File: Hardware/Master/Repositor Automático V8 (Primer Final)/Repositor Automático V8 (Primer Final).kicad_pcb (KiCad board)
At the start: 2 copper layers, 80.2 x 59.8 mm, 57 parts, among them IC1 TB67H450AFNG,EL, IC2 TB67H450AFNG,EL, IC3 TB67H450AFNG,EL, IC4 MP2307, J11 FdC, J2 UART, J3 Motor2, J4 Motor1, J5 Motor3, J6 Motor4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

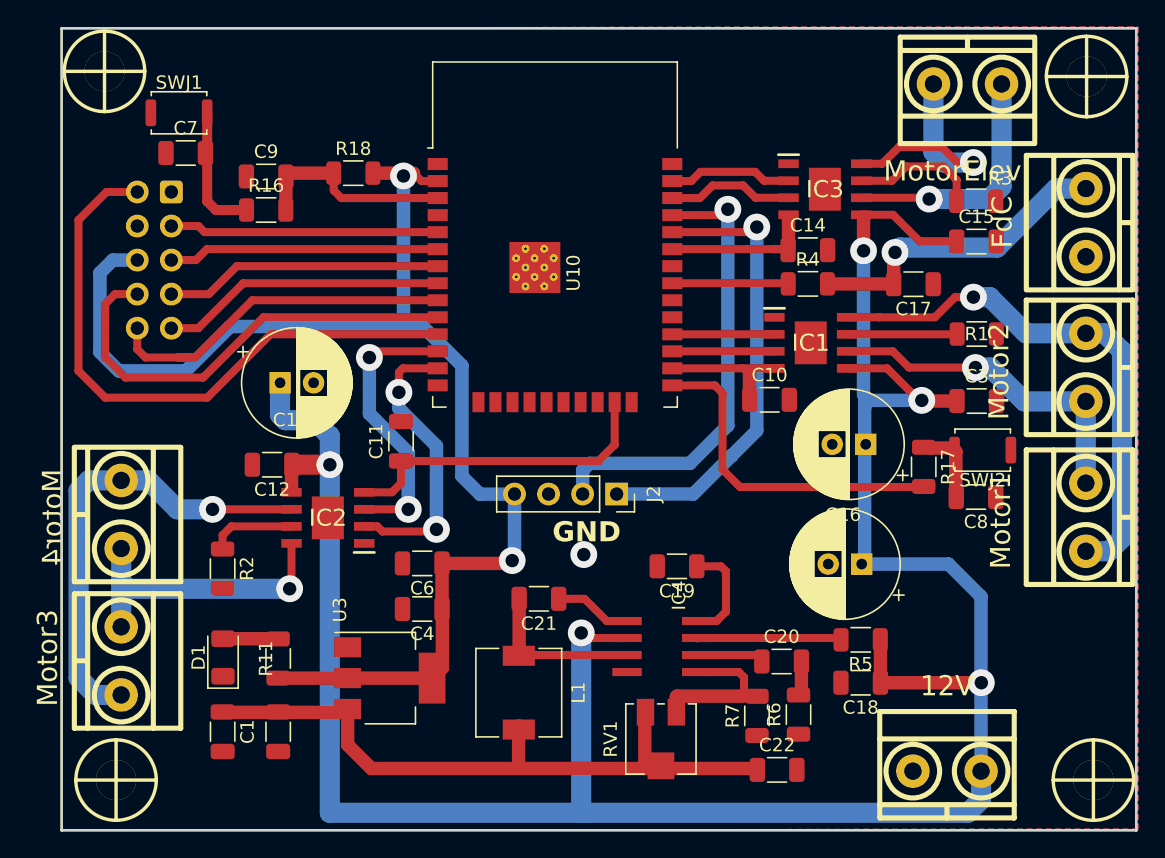
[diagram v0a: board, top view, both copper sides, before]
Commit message: Corrección de errores
Se agrego un Led de prueba para testear el funcionamiento del Esp32 WROOM y se corrigió la resistencia pull-up del pin BOOT
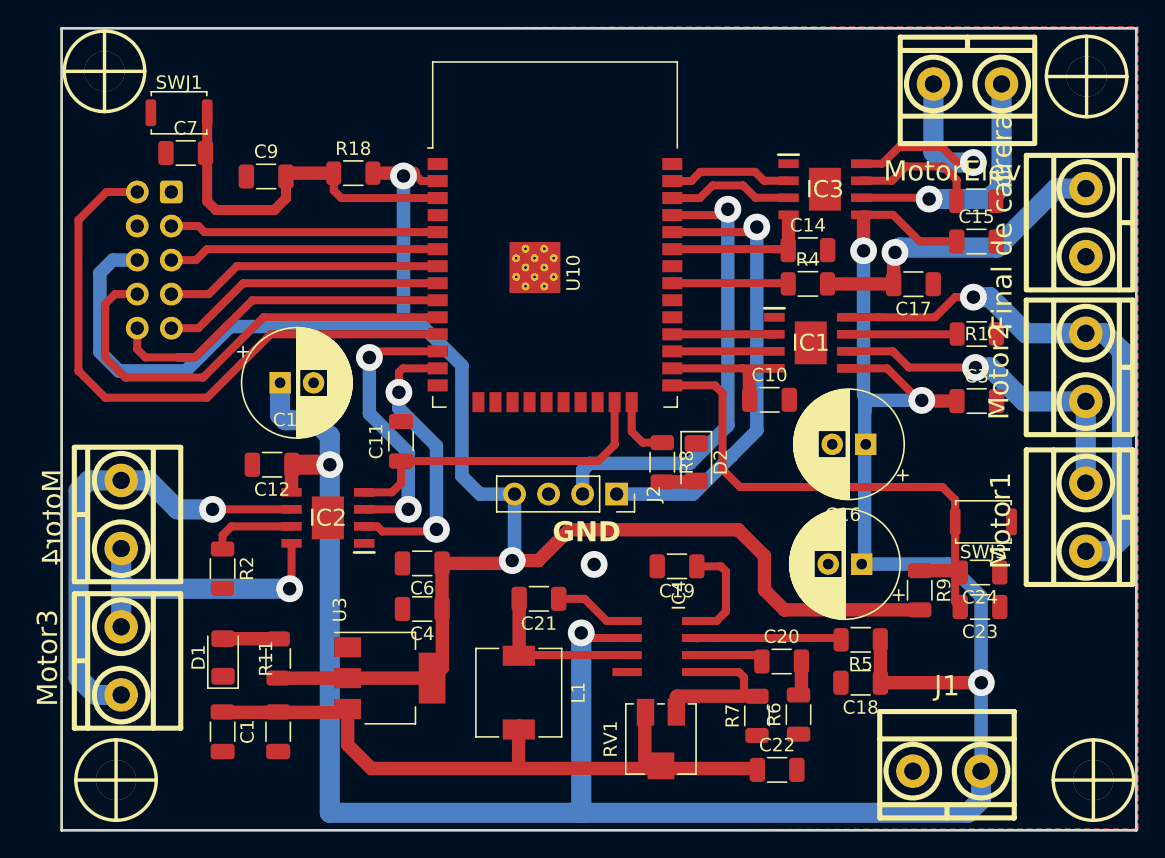
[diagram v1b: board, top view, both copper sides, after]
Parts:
- removed C8: 0.1u, Capacitor_SMD:C_1206_3216Metric
- removed R16, R17: 100k, Resistor_SMD:R_1206_3216Metric
- removed SWJ2: SW_MEC_5G, Button_Switch_SMD:SW_Push_SPST_NO_Alps_SKRK
- added C23: 0.1u, Capacitor_SMD:C_1206_3216Metric, F.Cu at (122.8, 81.3)
- added C24: 0.1u, Capacitor_SMD:C_1206_3216Metric, F.Cu at (122.8, 78.7)
- added D2: LED, LED_SMD:LED_1206_3216Metric, F.Cu at (101.6, 70.5)
- added R8: 330, Resistor_SMD:R_1206_3216Metric, F.Cu at (99.1, 70.5)
- added R9: 4.7k, Resistor_SMD:R_1206_3216Metric, F.Cu at (118.3, 80.0)
- added SWJ3: SW_MEC_5G, Button_Switch_SMD:SW_Push_SPST_NO_Alps_SKRK, F.Cu at (123.0, 74.9)
- J11: value FdC -> Final de carrera
- R18: value 10k -> 4.7k
- renumbered 12V to J1
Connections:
- C7 pad 2: Net-(SWJ1-B) -> /EN
- SWJ1 pad 2: Net-(SWJ1-B) -> /EN
- U10 pad 24: unconnected-(U10-IO2-Pad24) -> /Led prueba
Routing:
- net /3V3: track 99.1 -> 134.4 mm
- net /BOOT: track 25.2 -> 39.6 mm
- net /EN: track 15.0 -> 27.7 mm
- net Net-(SWJ1-B): track 9.81 -> 0.00 mm
- net Net-(SWJ2-B): track 5.49 -> 0.00 mm
- net /Led prueba: track 0.00 -> 4.82 mm
- net Net-(D2-A): track 0.00 -> 2.57 mm
- net /Vin: track 188.7 -> 188.2 mm

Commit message: Diseño final con correccion de Errores
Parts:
- removed hole_3mm (x4): VAL**, EESTN5:hole_3mm
- moved R4 13.5 mm to (123.4, 57.9), turned to 180 degrees
- moved R9 5.88 mm to (122.8, 83.8), turned to 0 degrees
- moved C3 2.66 mm to (122.5, 68.6)
- moved R1 2.07 mm to (122.5, 63.0)
- moved C17 0.71 mm to (117.9, 57.9), turned to 0 degrees
- moved C15 0.68 mm to (122.5, 53.3)
- moved R3 0.23 mm to (122.4, 50.8)
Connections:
- C17 pad 2: Net-(J11-Pin_1) -> /FC
- J11 pad 1: Net-(J11-Pin_1) -> /FC
- R4 pad 1: /FC -> /3V3
- R4 pad 2: Net-(J11-Pin_1) -> /FC
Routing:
- net /3V3: track 134.4 -> 175.2 mm
- net /FC: track 8.67 -> 38.6 mm, vias 0 -> 1
- net Net-(J11-Pin_1): track 23.6 -> 0.00 mm, vias 1 -> 0
- net /Vin: track 188.2 -> 190.6 mm
- net Net-(IC1-OUT2): track 40.0 -> 37.9 mm
- net Net-(IC1-RS): track 8.21 -> 9.05 mm
- net GND: vias 1 -> 2

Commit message: Correccion de errores diseño final
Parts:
- added hole_3mm: VAL**, EESTN5:hole_3mm, F.Cu at (58.3, 94.2)
- added hole_3mm: VAL**, EESTN5:hole_3mm, F.Cu at (131.2, 94.2)
- added hole_3mm: VAL**, EESTN5:hole_3mm, F.Cu at (57.5, 41.3)
- added hole_3mm: VAL**, EESTN5:hole_3mm, F.Cu at (130.7, 41.7)
- moved R4 13.5 mm to (109.9, 57.2), turned to 0 degrees
- moved R9 5.88 mm to (118.3, 80.0), turned to -90 degrees
- moved C3 2.66 mm to (122.5, 65.9)
- moved R1 2.07 mm to (122.5, 60.9)
- moved C17 0.71 mm to (117.8, 57.2), turned to 180 degrees
- moved C15 0.68 mm to (122.5, 54.0)
- moved R3 0.23 mm to (122.5, 51.0)
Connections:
- C17 pad 2: /FC -> Net-(J11-Pin_1)
- J11 pad 1: /FC -> Net-(J11-Pin_1)
- R4 pad 1: /3V3 -> /FC
- R4 pad 2: /FC -> Net-(J11-Pin_1)
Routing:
- net /3V3: track 175.2 -> 134.4 mm
- net /FC: track 38.6 -> 8.67 mm, vias 1 -> 0
- net Net-(J11-Pin_1): track 0.00 -> 23.6 mm, vias 0 -> 1
- net /Vin: track 190.6 -> 188.2 mm
- net Net-(IC1-OUT2): track 37.9 -> 40.0 mm
- net Net-(IC1-RS): track 9.05 -> 8.21 mm
- net GND: vias 2 -> 1

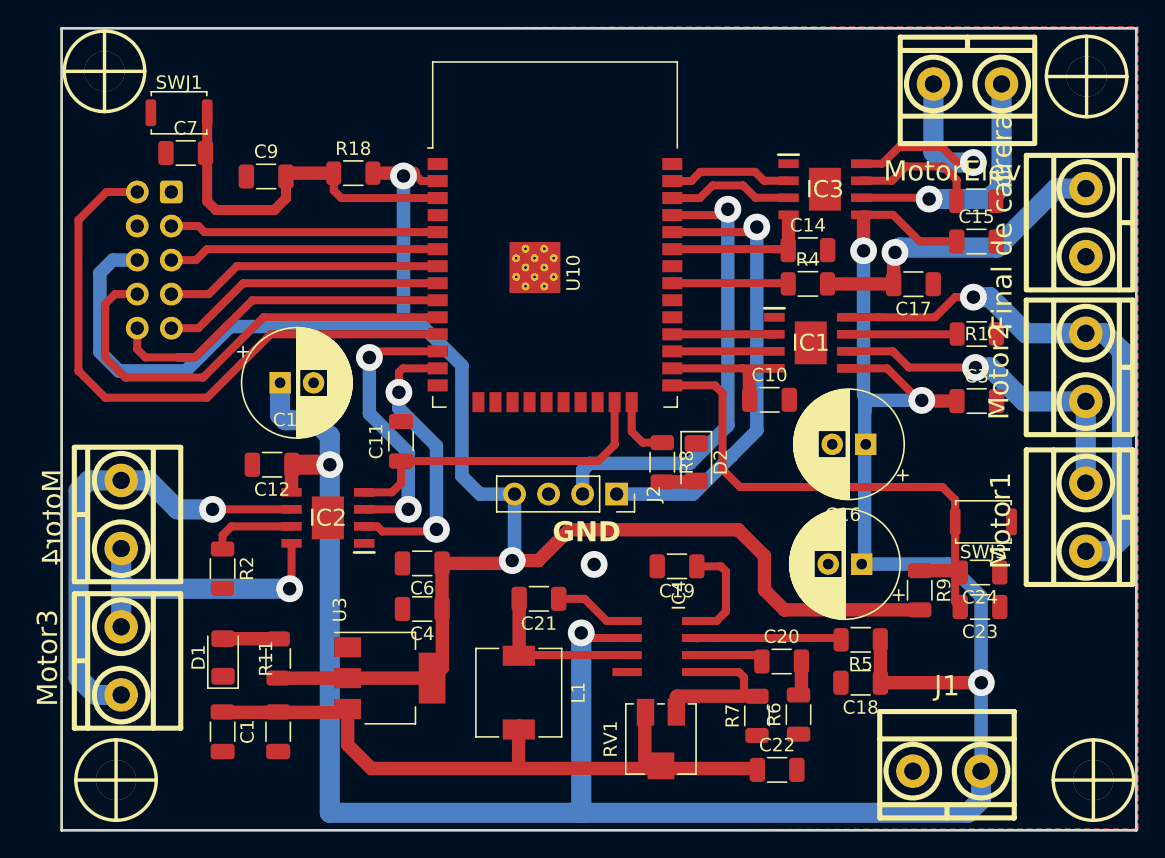
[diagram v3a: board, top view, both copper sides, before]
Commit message: Correccion IDC
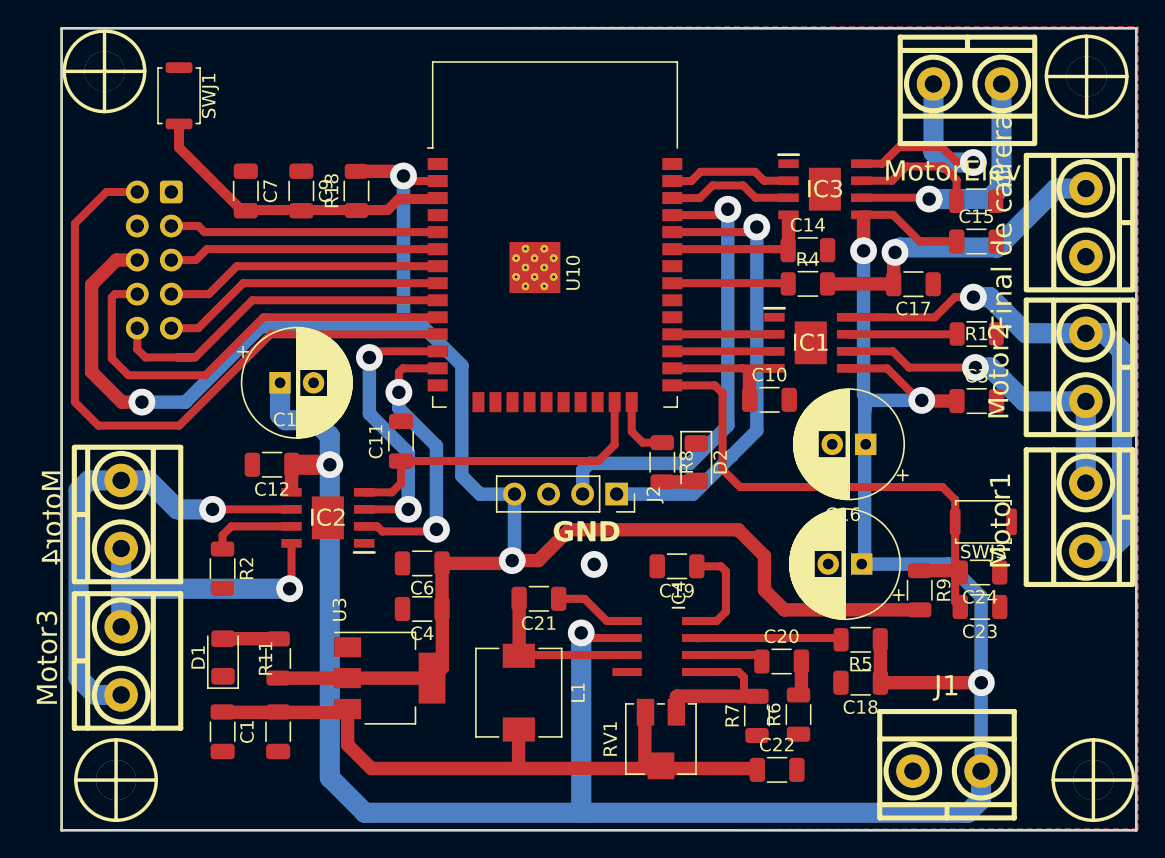
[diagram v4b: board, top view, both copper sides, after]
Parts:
- moved C7 5.30 mm to (68.0, 50.2), turned to -90 degrees
- moved C9 2.84 mm to (72.1, 50.2), turned to -90 degrees
- moved R18 1.35 mm to (76.2, 50.2), turned to 90 degrees
- moved SWJ1 1.27 mm to (63.0, 43.1), turned to -90 degrees
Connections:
- J8 pad 8: /Sen1 -> /3V3
- U10 pad 10: /Sen1 -> /3V3
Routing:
- net /3V3: track 134.4 -> 172.3 mm, vias 2 -> 3
- net /Sen1: track 34.0 -> 0.00 mm
- net /EN: track 27.7 -> 23.4 mm
- net /Sen7: track 46.1 -> 49.6 mm
- net /Vin: track 188.2 -> 186.7 mm

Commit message: Correccion Serigrafía
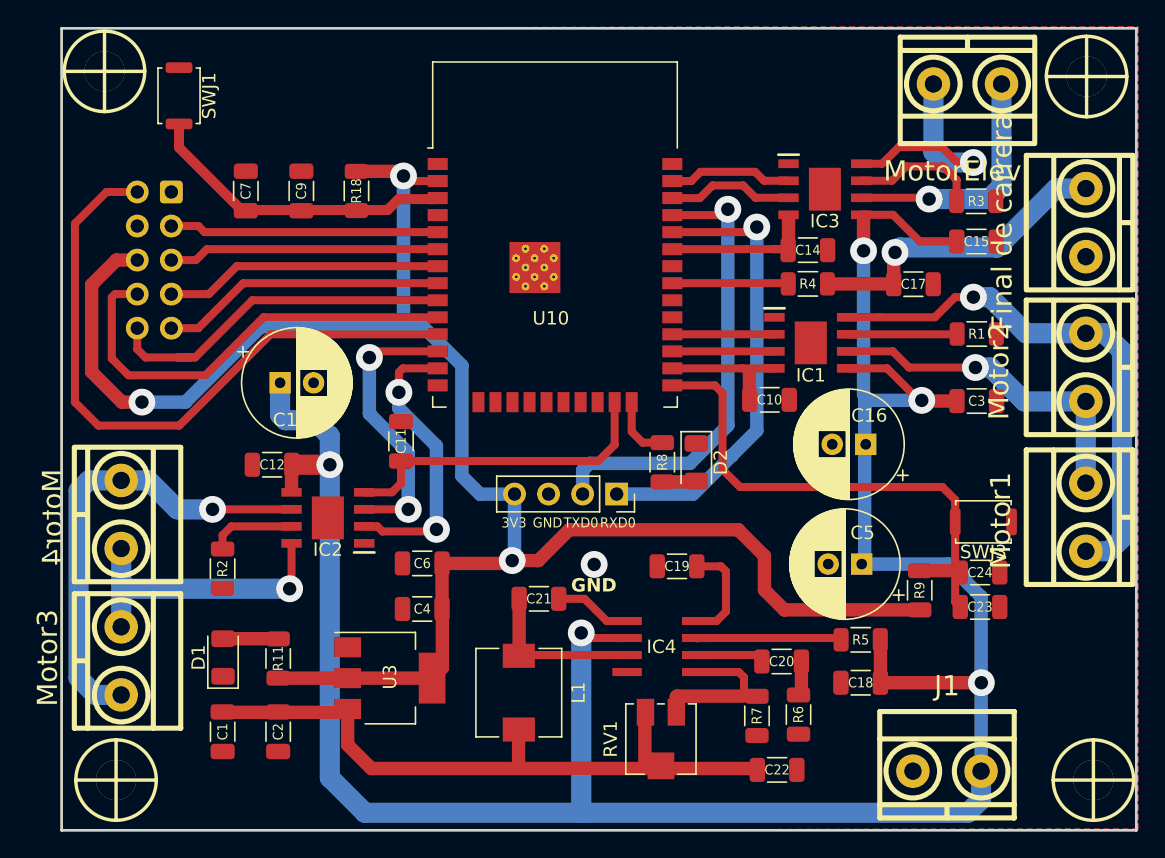
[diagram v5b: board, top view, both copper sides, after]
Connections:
- J8 pad 8: /3V3 -> /Sen1
- U10 pad 10: /3V3 -> /Sen1
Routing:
- net /Sen1: track 0.00 -> 33.2 mm
- net /3V3: track 172.3 -> 139.1 mm
